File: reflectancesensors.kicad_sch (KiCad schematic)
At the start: 10 parts, among them J1 Power, J2 Outputs, U1 TCRT5000L, U3 TCRT5000L

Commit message: some small changes
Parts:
- added H1, H2, H3, H4: MountingHole, MountingHole:MountingHole_3.2mm_M3_DIN965, symbol Mechanical:MountingHole
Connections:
- no-connect marks 0 -> 2

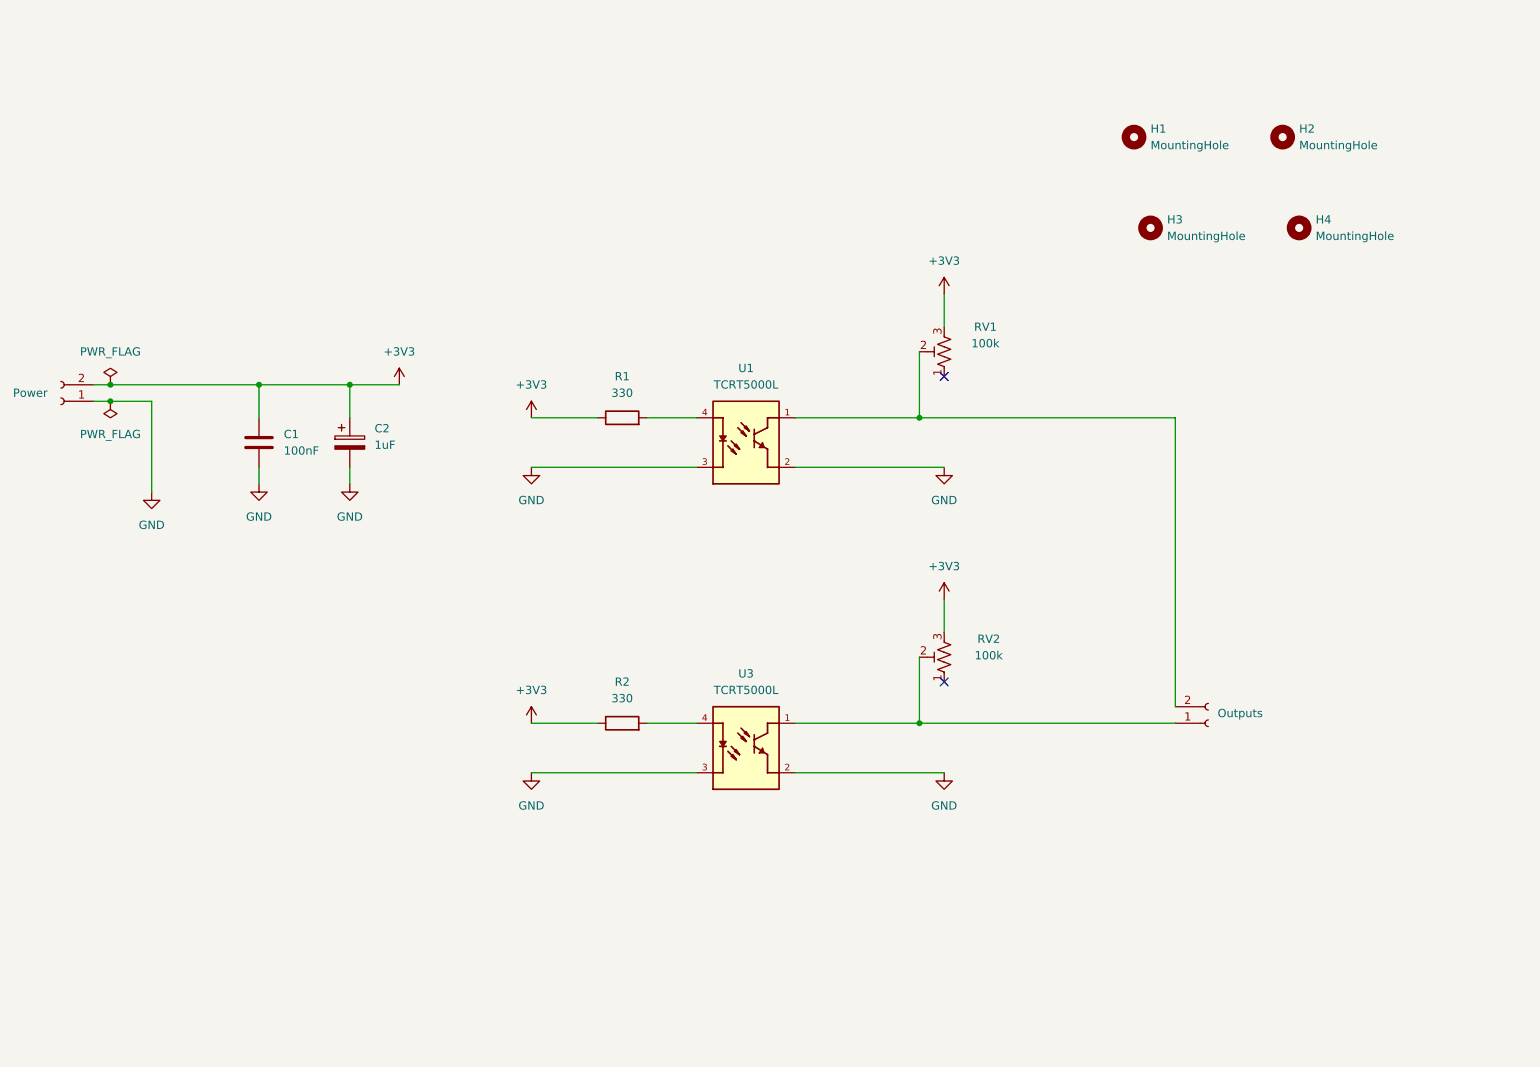
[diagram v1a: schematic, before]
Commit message: adding high power reflectance
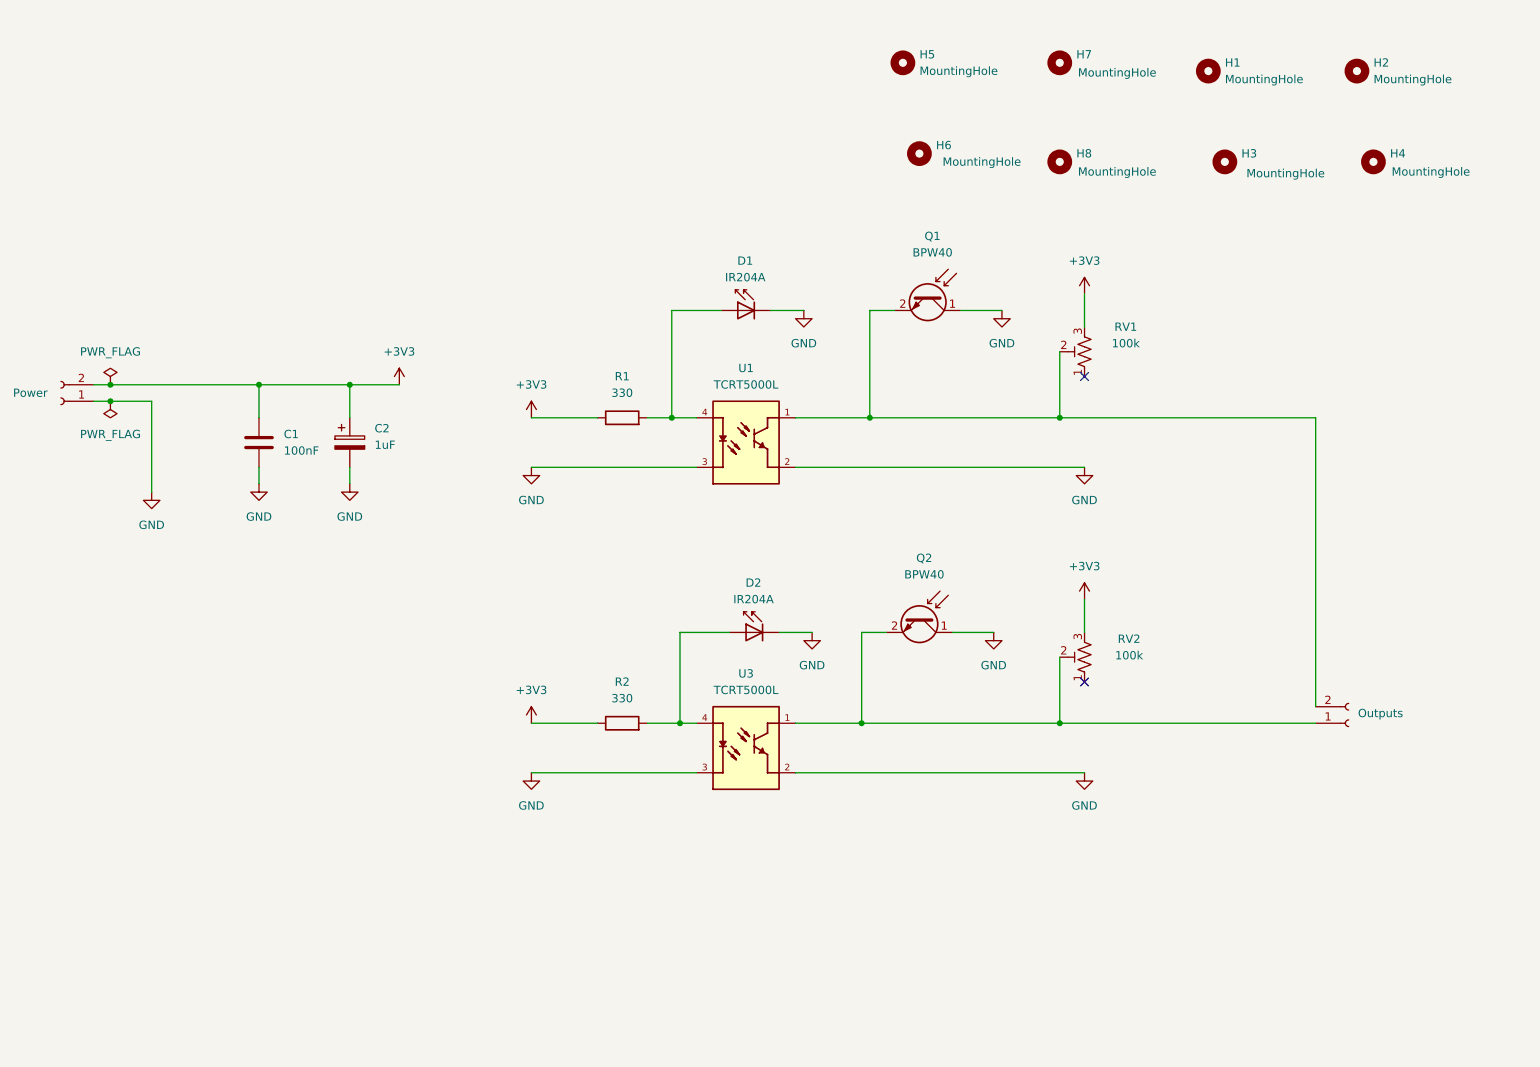
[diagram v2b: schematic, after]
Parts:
- added D1, D2: IR204A, LED_THT:LED_D3.0mm_IRBlack, symbol LED:IR204A
- added H5, H6, H7, H8: MountingHole, MountingHole:MountingHole_3.2mm_M3_DIN965, symbol Mechanical:MountingHole
- added Q1, Q2: BPW40, LED_THT:LED_D5.0mm_Clear, symbol Sensor_Optical:BPW40
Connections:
- net GND: now also D1.1 (K), D2.1 (K), Q1.1 (C), Q2.1 (C)
- net at J2.2 (Pin_2), RV1.2, U1.1: now also Q1.2 (E)
- net at R1.2, U1.4: now also D1.2 (A)
- net at R2.2, U3.4: now also D2.2 (A)
- net at J2.1 (Pin_1), RV2.2, U3.1: now also Q2.2 (E)
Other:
- moved on the sheet: H1, H2, H3, H4, RV1, RV2

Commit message: small changes
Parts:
- removed H1, H2, H3, H4: MountingHole, MountingHole:MountingHole_3.2mm_M3_DIN965, symbol Mechanical:MountingHole
- D1, D2: footprint LED_THT:LED_D3.0mm_IRBlack -> LED_THT:LED_D5.0mm
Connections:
- net GND: now also Q1.2 (E), Q2.2 (E); no longer Q1.1 (C), Q2.1 (C)
- net at J2.2 (Pin_2), RV1.2, U1.1: now also Q1.1 (C); no longer Q1.2 (E)
- net at J2.1 (Pin_1), RV2.2, U3.1: now also Q2.1 (C); no longer Q2.2 (E)
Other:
- moved on the sheet: H5, H6, H7, H8, Q1, Q2

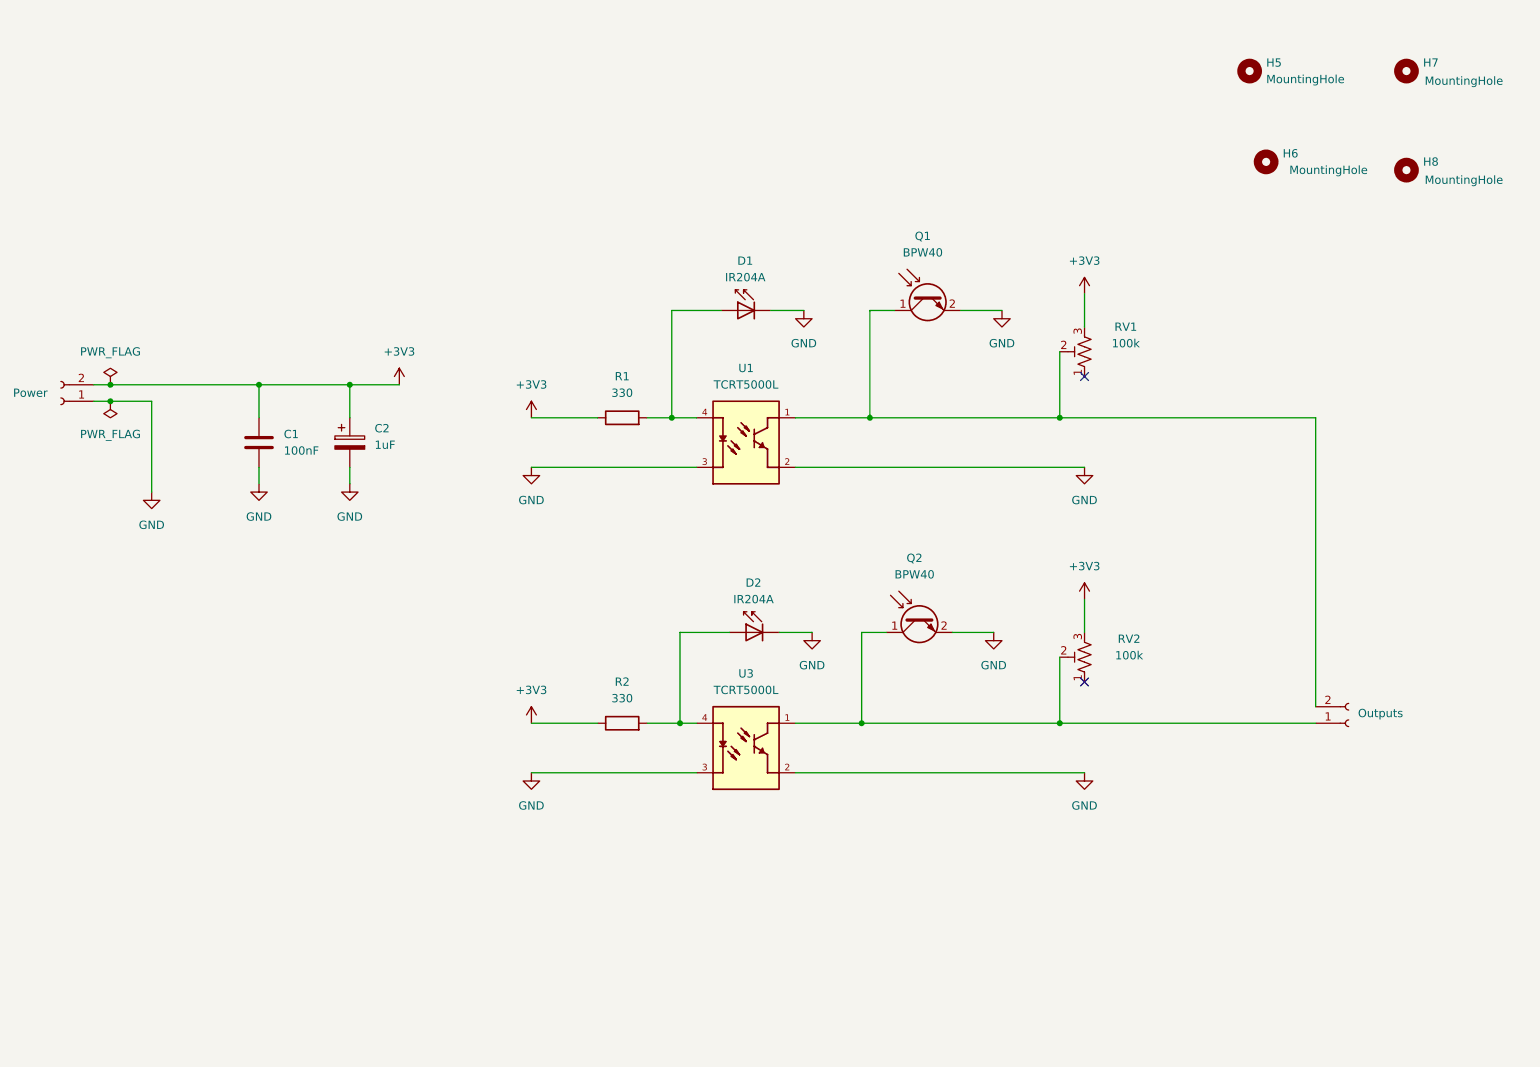
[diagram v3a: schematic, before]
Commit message: Update reflectancesensors.kicad_sch
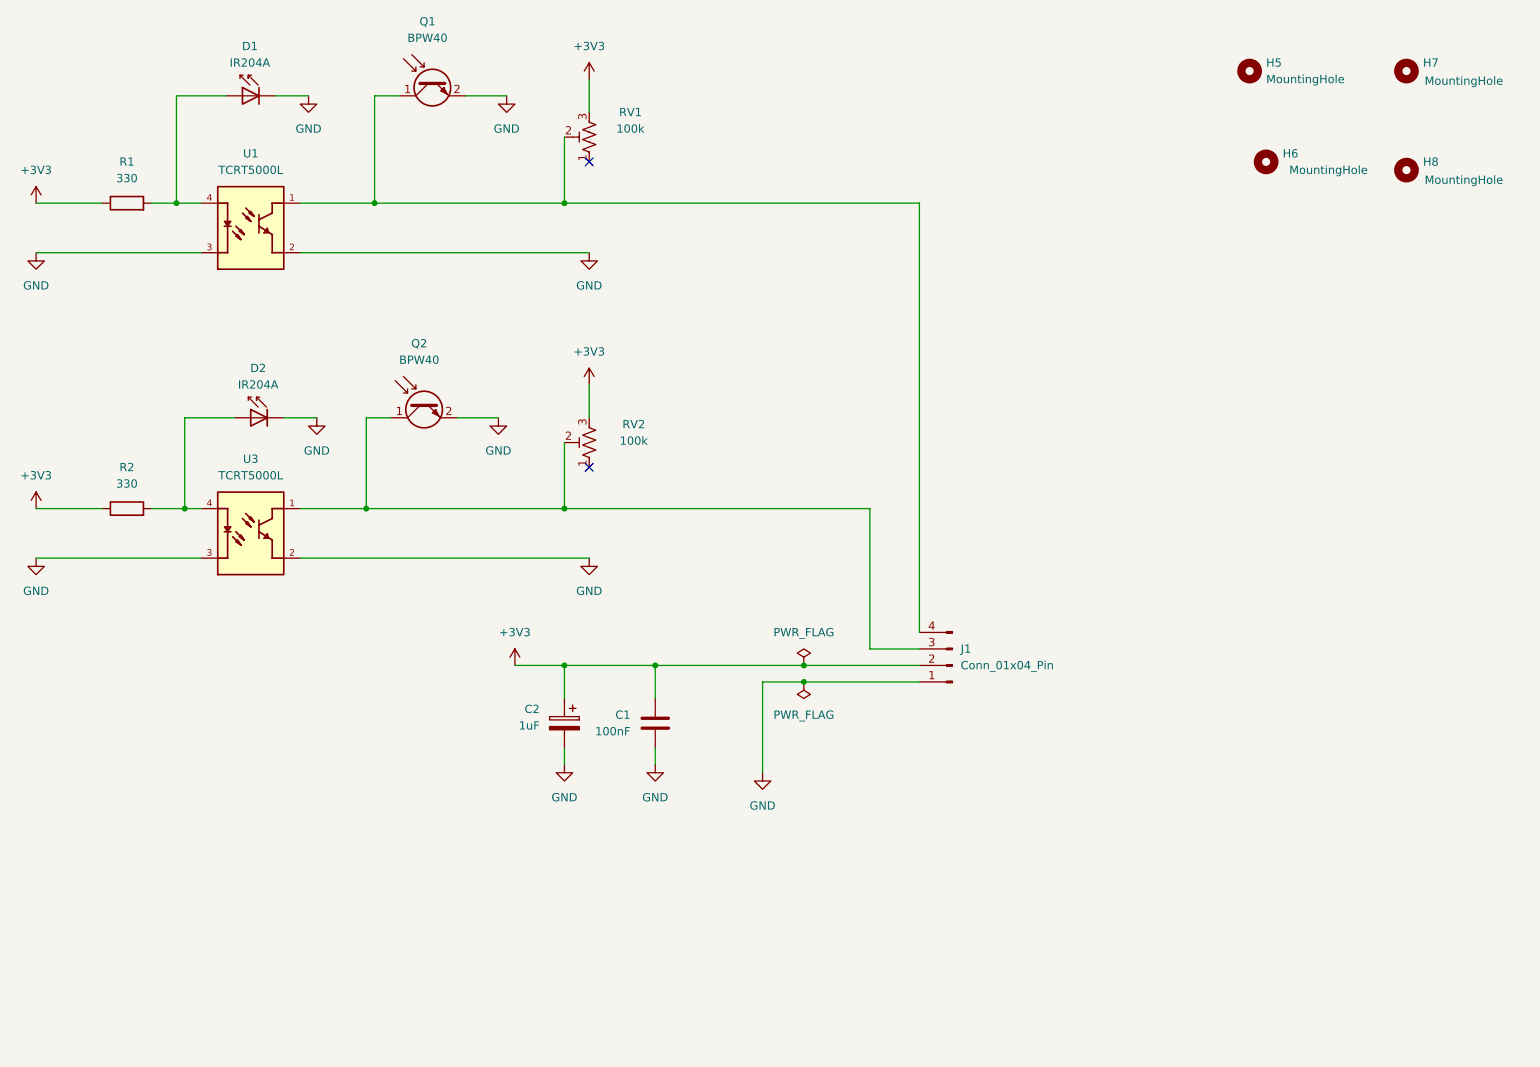
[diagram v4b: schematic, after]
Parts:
- removed J1: Power, Connector_JST:JST_XH_B2B-XH-A_1x02_P2.50mm_Vertical, symbol Connector:Conn_01x02_Socket
- removed J2: Outputs, Connector_JST:JST_XH_B2B-XH-A_1x02_P2.50mm_Vertical, symbol Connector:Conn_01x02_Socket
- added J1: Conn_01x04_Pin, Connector_JST:JST_EH_S4B-EH_1x04_P2.50mm_Horizontal, symbol Connector:Conn_01x04_Pin
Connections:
- net +3V3: now also J1.2 (Pin_2)
- net GND: now also J1.1 (Pin_1)
- net at Q1.1 (C), RV1.2, U1.1: now also J1.4 (Pin_4)
- net at Q2.1 (C), RV2.2, U3.1: now also J1.3 (Pin_3)
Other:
- moved on the sheet: C1, C2, D1, D2, Q1, Q2, R1, R2, RV1, RV2, U1, U3

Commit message: changing connector
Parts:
- removed J1: Conn_01x04_Pin, Connector_JST:JST_EH_S4B-EH_1x04_P2.50mm_Horizontal, symbol Connector:Conn_01x04_Pin
- added J2: Conn_01x04_Socket, Connector_JST:JST_XH_S4B-XH-A-1_1x04_P2.50mm_Horizontal, symbol Connector:Conn_01x04_Socket
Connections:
- net +3V3: now also J2.1 (Pin_1)
- net GND: now also J2.4 (Pin_4)
- net at Q1.1 (C), RV1.2, U1.1: now also J2.2 (Pin_2)
- net at Q2.1 (C), RV2.2, U3.1: now also J2.3 (Pin_3)
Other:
- moved on the sheet: C1, C2, D1, D2, H5, H6, H7, H8, Q1, Q2, R1, R2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
